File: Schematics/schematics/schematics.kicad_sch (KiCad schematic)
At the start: 14 parts, among them SW1 POWER_SWITCH, U1 ESP32-S3-DEVKITC-1-N16R8

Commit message: continue working on the schematics
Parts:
- removed MC6RE_V1: ~, symbol mario:MC6RE_V2
- removed MOTOR_BRUSHLESS1, MOTOR_BRUSHLESS2: ~, symbol mario:MOTOR_BRUSSLESS
- added LED1: GREEN, symbol Device:LED
- added LED2: RED, symbol Device:LED
- added LED3: BLUE, symbol Device:LED
- added MOTOR_BRUSHLESS_LEFT, MOTOR_BRUSHLESS_RIGHT: ~, symbol mario:MOTOR_BRUSSLESS
- added RECEIVER_MC6RE: ~, symbol mario:MC6RE
- renumbered CON_BAT1 to CON_BAT, ZS-X11 to ZS-X11_RIGHT, ZS-X1 to ZS-X1_LEFT
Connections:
- net 5V: now also U1. (GND); no longer U1.J1_21 (5Vin), ZS-X11_RIGHT. (ANALOG_CTRL), ZS-X1_LEFT. (ANALOG_CTRL)
- net ENC_A_LEFT: now also E6B2-CWZ6C_LEFT. (GND)
- net ENC_A_RIGHT: now also E6B2-CWZ6C_RIGHT. (GND)
- net ENC_B_LEFT: now also E6B2-CWZ6C_LEFT. (GND)
- net ENC_B_RIGHT: now also E6B2-CWZ6C_RIGHT. (GND)
- net Earth: now also U1. (GND), LED1.1 (K), LED2.1 (K), LED3.1 (K); no longer U1.J1_16 (GPIO10), U1.J1_5 (GPIO5), U1.J3_21 (GND)
- net V_BAT: now also SEN0291. (GND)
- net TX2: now reaches WT901C1. (RX)
- net TX2: now also U1. (GND); no longer U1.J3_2 (U0TXD/GPIO43)
- net ZS-X11_PWM_LEFT: now reaches ZS-X1_LEFT. (ANALOG_CTRL)
- net WATT_SDA: now reaches SEN0291. (GND)
- net WATT_SDA: now also U1. (GND); no longer U1.J1_12 (GPIO8)
- net at CON_BAT. (GND): now also SEN0291. (GND)
- net ZS-X11_PWM_RIGHT: now reaches ZS-X11_RIGHT. (ANALOG_CTRL)
- new net: MOTOR_BRUSHLESS_RIGHT. (H_GND), ZS-X11_RIGHT. (ANALOG_CTRL) (x3)
- new net: MOTOR_BRUSHLESS_LEFT. (H_GND), ZS-X1_LEFT. (ANALOG_CTRL) (x3)
- new net HA_LEFT: MOTOR_BRUSHLESS_LEFT. (H_GND), ZS-X1_LEFT. (ANALOG_CTRL)
- new net HA_RIGHT: MOTOR_BRUSHLESS_RIGHT. (H_GND), ZS-X11_RIGHT. (ANALOG_CTRL)
- new net HB_LEFT: MOTOR_BRUSHLESS_LEFT. (H_GND), ZS-X1_LEFT. (ANALOG_CTRL)
- new net HB_RIGHT: MOTOR_BRUSHLESS_RIGHT. (H_GND), ZS-X11_RIGHT. (ANALOG_CTRL)
- new net HC_LEFT: MOTOR_BRUSHLESS_LEFT. (H_GND), ZS-X1_LEFT. (ANALOG_CTRL)
- new net HC_RIGHT: MOTOR_BRUSHLESS_RIGHT. (H_GND), ZS-X11_RIGHT. (ANALOG_CTRL)
- new net H_5V_LEFT: MOTOR_BRUSHLESS_LEFT. (H_GND), ZS-X1_LEFT. (ANALOG_CTRL)
- new net H_5V_RIGHT: MOTOR_BRUSHLESS_RIGHT. (H_GND), ZS-X11_RIGHT. (ANALOG_CTRL)
- new net H_GND_LEFT: MOTOR_BRUSHLESS_LEFT. (H_GND), ZS-X1_LEFT. (ANALOG_CTRL)
- new net H_GND_RIGHT: MOTOR_BRUSHLESS_RIGHT. (H_GND), ZS-X11_RIGHT. (ANALOG_CTRL)
- new net LED1: LED1.2 (A)
- new net LED2: LED2.2 (A)
- new net LED3: LED3.2 (A)
- new net RX2: U1. (GND), WT901C1. (RX)
- new net WATT_SCL: SEN0291. (GND), U1. (GND)
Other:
- moved on the sheet: LM2596, WT901C1, ZS-X11_RIGHT, ZS-X1_LEFT

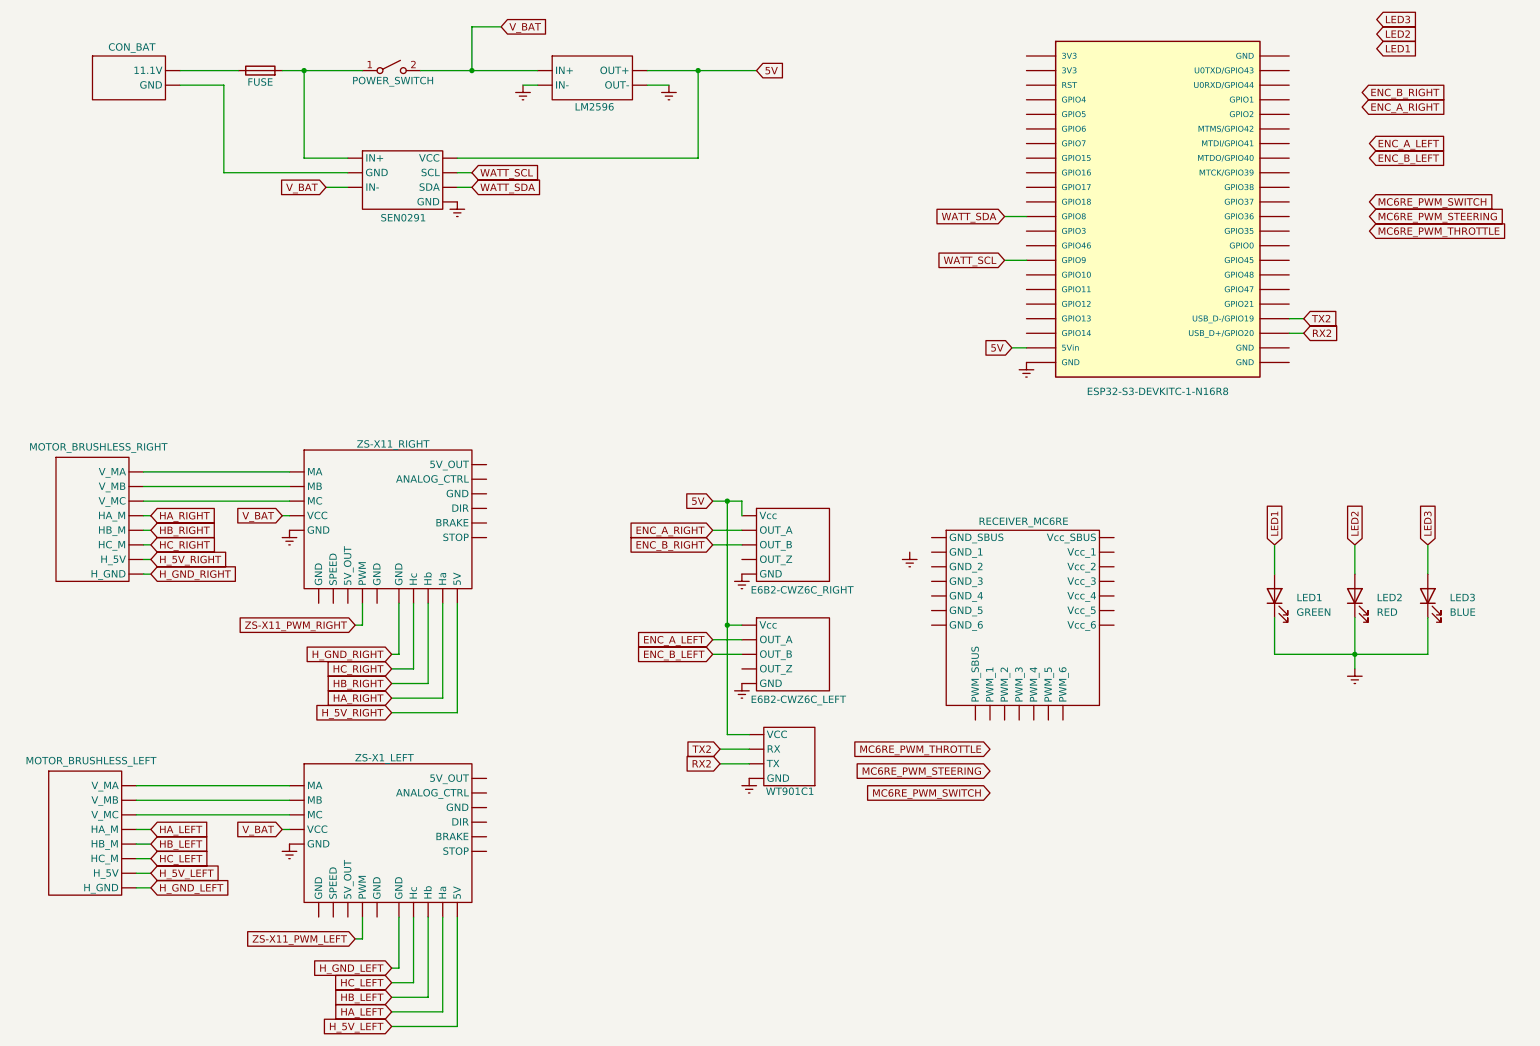
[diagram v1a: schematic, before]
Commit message: add footprints and names
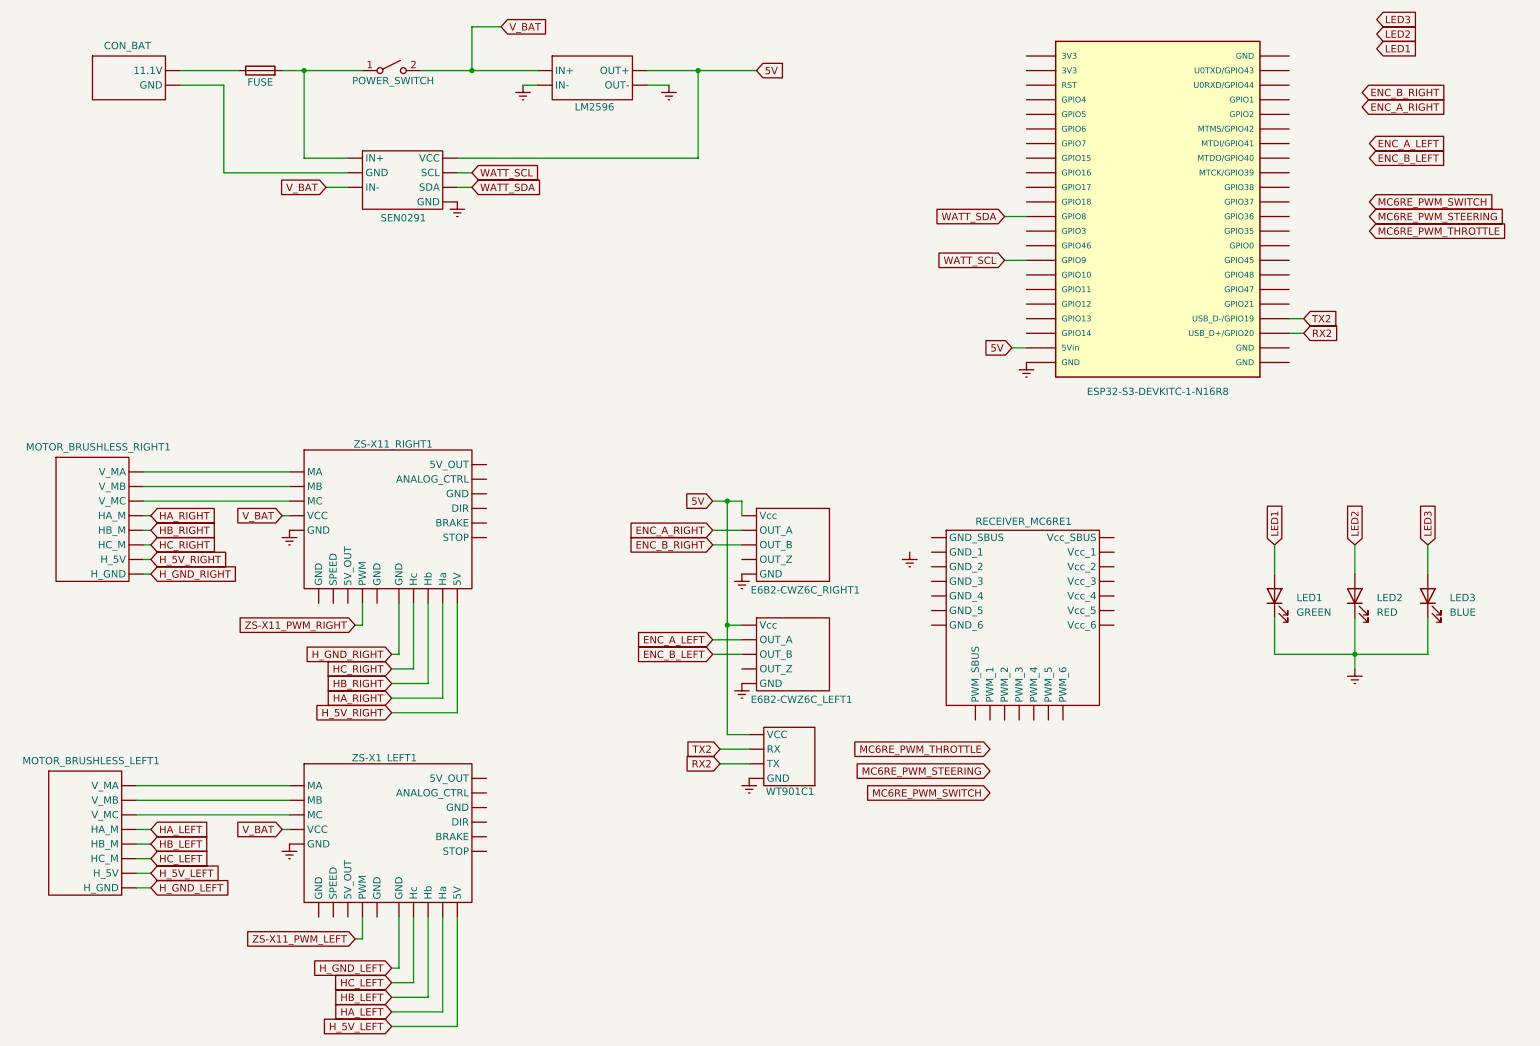
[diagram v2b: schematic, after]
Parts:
- CON_BAT: footprint (none) -> Connector_AMASS:AMASS_XT60-F_1x02_P7.20mm_Vertical
- F1, SW1: footprint (none) -> TestPoint:TestPoint_Bridge_Pitch2.0mm_Drill0.7mm
- LED1, LED2, LED3: footprint (none) -> LED_THT:LED_D3.0mm
- renumbered E6B2-CWZ6C_LEFT to E6B2-CWZ6C_LEFT1, E6B2-CWZ6C_RIGHT to E6B2-CWZ6C_RIGHT1, MOTOR_BRUSHLESS_LEFT to MOTOR_BRUSHLESS_LEFT1, MOTOR_BRUSHLESS_RIGHT to MOTOR_BRUSHLESS_RIGHT1, RECEIVER_MC6RE to RECEIVER_MC6RE1, ZS-X11_RIGHT to ZS-X11_RIGHT1, ZS-X1_LEFT to ZS-X1_LEFT1
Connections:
- new net: MOTOR_BRUSHLESS_RIGHT1. (H_GND), ZS-X11_RIGHT1. (ANALOG_CTRL) (x3)
- new net: MOTOR_BRUSHLESS_LEFT1. (H_GND), ZS-X1_LEFT1. (ANALOG_CTRL) (x3)
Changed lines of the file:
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@@
 		(on_board yes)
 		(dnp no)
-		(property "Reference" "RECEIVER_MC6RE"
+		(property "Reference" "RECEIVER_MC6RE1"
 			(at 188.722 107.696 0)
 			(effects
@@
 			(project ""
 				(path "/29c96457-b859-4d59-aaa2-52833e6eb6f5"
-					(reference "RECEIVER_MC6RE")
+					(reference "RECEIVER_MC6RE1")
 					(unit 1)
 				)
@@
 		(on_board yes)
 		(dnp no)
-		(property "Reference" "MOTOR_BRUSHLESS_RIGHT"
+		(property "Reference" "MOTOR_BRUSHLESS_RIGHT1"
 			(at 27.686 94.742 0)
 			(effects
@@
 			(project "schematics"
 				(path "/29c96457-b859-4d59-aaa2-52833e6eb6f5"
-					(reference "MOTOR_BRUSHLESS_RIGHT")
+					(reference "MOTOR_BRUSHLESS_RIGHT1")
 					(unit 1)
 				)
@@
 		(on_board yes)
 		(dnp no)
-		(property "Reference" "MOTOR_BRUSHLESS_LEFT"
+		(property "Reference" "MOTOR_BRUSHLESS_LEFT1"
 			(at 26.416 149.352 0)
 			(effects
@@
 			(project "schematics"
 				(path "/29c96457-b859-4d59-aaa2-52833e6eb6f5"
-					(reference "MOTOR_BRUSHLESS_LEFT")
+					(reference "MOTOR_BRUSHLESS_LEFT1")
 					(unit 1)
 				)
@@
 		(dnp no)
 		(fields_autoplaced yes)
-		(property "Reference" "#PWR09"
+		(property "Reference" "#PWR010"
 			(at 189.23 86.36 0)
 			(effects
@@
 			(project "schematics"
 				(path "/29c96457-b859-4d59-aaa2-52833e6eb6f5"
-					(reference "#PWR09")
+					(reference "#PWR010")
 					(unit 1)
 				)
@@
 		(dnp no)
 		(fields_autoplaced yes)
-		(property "Reference" "#PWR04"
+		(property "Reference" "#PWR05"
 			(at 127 38.1 0)
 			(effects
@@
 			(project "schematics"
 				(path "/29c96457-b859-4d59-aaa2-52833e6eb6f5"
-					(reference "#PWR04")
+					(reference "#PWR05")
 					(unit 1)
 				)
@@
 		(on_board yes)
 		(dnp no)
-		(property "Reference" "E6B2-CWZ6C_RIGHT"
+		(property "Reference" "E6B2-CWZ6C_RIGHT1"
 			(at 141.224 119.634 0)
 			(effects
@@
 			(project ""
 				(path "/29c96457-b859-4d59-aaa2-52833e6eb6f5"
-					(reference "E6B2-CWZ6C_RIGHT")
+					(reference "E6B2-CWZ6C_RIGHT1")
 					(unit 1)
 				)
@@
 		(dnp no)
 		(fields_autoplaced yes)
-		(property "Reference" "#PWR08"
+		(property "Reference" "#PWR03"
 			(at 90.17 58.42 0)
 			(effects
@@
 			(project "schematics"
 				(path "/29c96457-b859-4d59-aaa2-52833e6eb6f5"
-					(reference "#PWR08")
+					(reference "#PWR03")
 					(unit 1)
 				)
@@
 			)
 		)
-		(property "Footprint" ""
+		(property "Footprint" "LED_THT:LED_D3.0mm"
 			(at 259.08 120.65 0)
 			(effects
@@
 		(dnp no)
 		(fields_autoplaced yes)
-		(property "Reference" "#PWR02"
+		(property "Reference" "#PWR06"
 			(at 139.7 123.19 0)
 			(effects
@@
 			(project "schematics"
 				(path "/29c96457-b859-4d59-aaa2-52833e6eb6f5"
-					(reference "#PWR02")
+					(reference "#PWR06")
 					(unit 1)
 				)
@@
 			)
 		)
-		(property "Footprint" ""
+		(property "Footprint" "TestPoint:TestPoint_Bridge_Pitch2.0mm_Drill0.7mm"
 			(at 78.74 29.21 0)
 			(effects
@@
 		(dnp no)
 		(fields_autoplaced yes)
-		(property "Reference" "#PWR012"
+		(property "Reference" "#PWR011"
 			(at 246.38 139.7 0)
 			(effects
@@
 			(project "schematics"
 				(path "/29c96457-b859-4d59-aaa2-52833e6eb6f5"
-					(reference "#PWR012")
+					(reference "#PWR011")
 					(unit 1)
 				)
@@
 			)
 		)
-		(property "Footprint" ""
+		(property "Footprint" "TestPoint:TestPoint_Bridge_Pitch2.0mm_Drill0.7mm"
 			(at 55.88 30.988 90)
 			(effects
@@
 		(on_board yes)
 		(dnp no)
-		(property "Reference" "ZS-X1_LEFT"
+		(property "Reference" "ZS-X1_LEFT1"
 			(at 77.47 148.844 0)
 			(effects
@@
 			(project ""
 				(path "/29c96457-b859-4d59-aaa2-52833e6eb6f5"
-					(reference "ZS-X1_LEFT")
+					(reference "ZS-X1_LEFT1")
 					(unit 1)
 				)
@@
 		(on_board yes)
 		(dnp no)
-		(fields_autoplaced yes)
 		(property "Reference" "CON_BAT"
-			(at 33.528 25.146 0)
+			(at 32.766 24.892 0)
 			(effects
 				(font
@@
 		)
 		(property "Value" "~"
-			(at 31.75 25.4 0)
-			(effects
-				(font
-					(size 1.27 1.27)
-				)
-			)
-		)
-		(property "Footprint" ""
+			(at 33.02 25.4 0)
+			(effects
+				(font
+					(size 1.27 1.27)
+				)
+			)
+		)
+		(property "Footprint" "Connector_AMASS:AMASS_XT60-F_1x02_P7.20mm_Vertical"
 			(at 35.56 26.67 0)
 			(effects
@@
 			)
 		)
-		(property "Footprint" ""
+		(property "Footprint" "LED_THT:LED_D3.0mm"
 			(at 232.41 120.65 0)
 			(effects
@@
 		(dnp no)
 		(fields_autoplaced yes)
-		(property "Reference" "#PWR010"
+		(property "Reference" "#PWR01"
 			(at 60.96 115.57 0)
 			(effects
@@
 			(project "schematics"
 				(path "/29c96457-b859-4d59-aaa2-52833e6eb6f5"
-					(reference "#PWR010")
+					(reference "#PWR01")
 					(unit 1)
 				)
@@
 		(dnp no)
 		(fields_autoplaced yes)
-		(property "Reference" "#PWR07"
+		(property "Reference" "#PWR08"
 			(at 140.97 158.75 0)
 			(effects
@@
 			(project "schematics"
 				(path "/29c96457-b859-4d59-aaa2-52833e6eb6f5"
-					(reference "#PWR07")
+					(reference "#PWR08")
 					(unit 1)
 				)
@@
 		(dnp no)
 		(fields_autoplaced yes)
-		(property "Reference" "#PWR06"
+		(property "Reference" "#PWR09"
 			(at 168.91 119.38 0)
 			(effects
@@
 			(project "schematics"
 				(path "/29c96457-b859-4d59-aaa2-52833e6eb6f5"
-					(reference "#PWR06")
+					(reference "#PWR09")
 					(unit 1)
 				)
@@
 			)
 		)
-		(property "Footprint" ""
+		(property "Footprint" "LED_THT:LED_D3.0mm"
 			(at 246.38 120.65 0)
 			(effects
@@
 		(dnp no)
 		(fields_autoplaced yes)
-		(property "Reference" "#PWR011"
+		(property "Reference" "#PWR02"
 			(at 60.96 170.18 0)
 			(effects
@@
 			(project "schematics"
 				(path "/29c96457-b859-4d59-aaa2-52833e6eb6f5"
-					(reference "#PWR011")
+					(reference "#PWR02")
 					(unit 1)
 				)
@@
 		(on_board yes)
 		(dnp no)
-		(property "Reference" "E6B2-CWZ6C_LEFT"
+		(property "Reference" "E6B2-CWZ6C_LEFT1"
 			(at 141.224 138.684 0)
 			(effects
@@
 			(project "schematics"
 				(path "/29c96457-b859-4d59-aaa2-52833e6eb6f5"
-					(reference "E6B2-CWZ6C_LEFT")
+					(reference "E6B2-CWZ6C_LEFT1")
 					(unit 1)
 				)
@@
 		(dnp no)
 		(fields_autoplaced yes)
-		(property "Reference" "#PWR05"
+		(property "Reference" "#PWR07"
 			(at 139.7 142.24 0)
 			(effects
@@
 			(project "schematics"
 				(path "/29c96457-b859-4d59-aaa2-52833e6eb6f5"
-					(reference "#PWR05")
+					(reference "#PWR07")
 					(unit 1)
 				)
@@
 		(on_board yes)
 		(dnp no)
-		(property "Reference" "ZS-X11_RIGHT"
+		(property "Reference" "ZS-X11_RIGHT1"
 			(at 78.994 94.234 0)
 			(effects
@@
 			(project ""
 				(path "/29c96457-b859-4d59-aaa2-52833e6eb6f5"
-					(reference "ZS-X11_RIGHT")
+					(reference "ZS-X11_RIGHT1")
 					(unit 1)
 				)
@@
 		(dnp no)
 		(fields_autoplaced yes)
-		(property "Reference" "#PWR03"
+		(property "Reference" "#PWR04"
 			(at 101.6 38.1 0)
 			(effects
@@
 			(project "schematics"
 				(path "/29c96457-b859-4d59-aaa2-52833e6eb6f5"
-					(reference "#PWR03")
-					(unit 1)
-				)
+					(reference "#PWR04")
+					(unit 1)
+				)
